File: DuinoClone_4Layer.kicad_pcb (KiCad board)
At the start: 2 copper layers, 41.4 x 27.7 mm, 17 parts, among them J1 Digital pins, J2 Serial, J3 ICSP, J4 I2C, U1 DS1337S+, U2 24LC1025, U3 24LC1025, U4 ATMEGA328P-AU, Y1 Crystal 32MHz, Y2 Crystal 16MHz

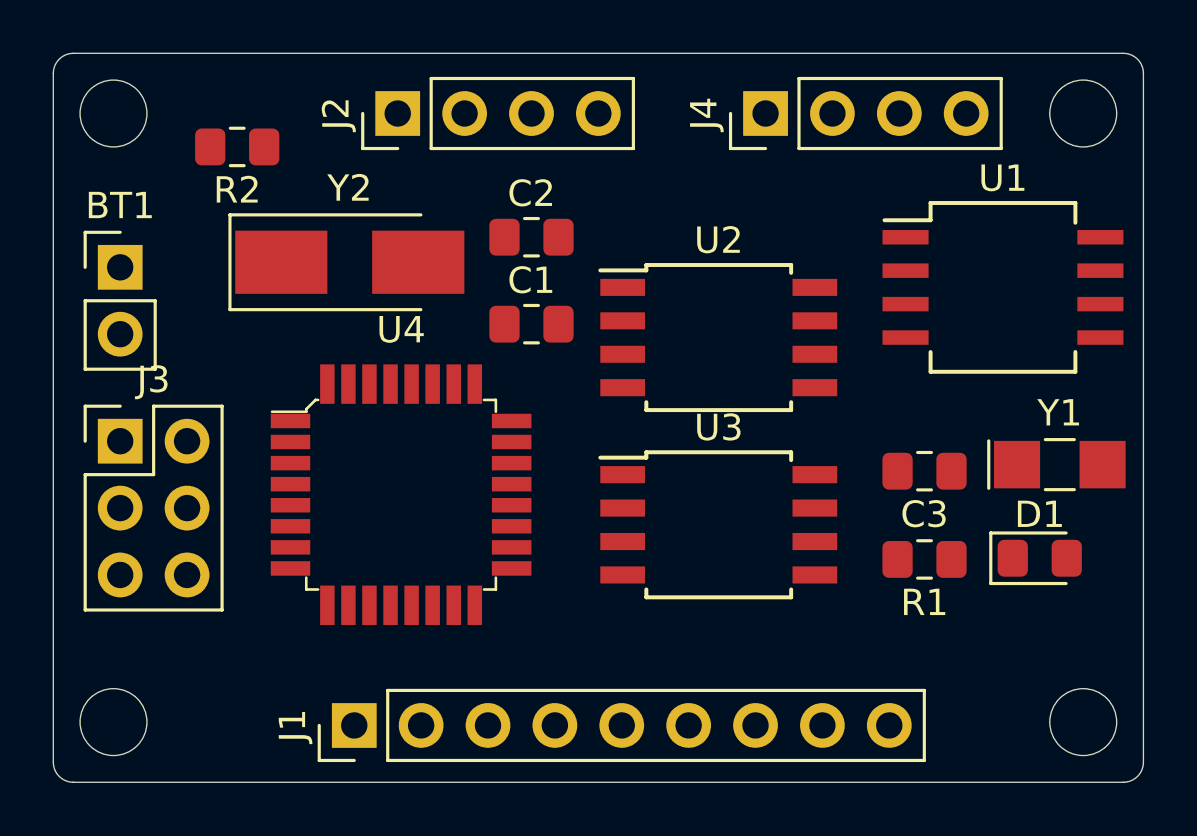
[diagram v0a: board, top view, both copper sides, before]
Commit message: Created copper filled area for 2-layer board
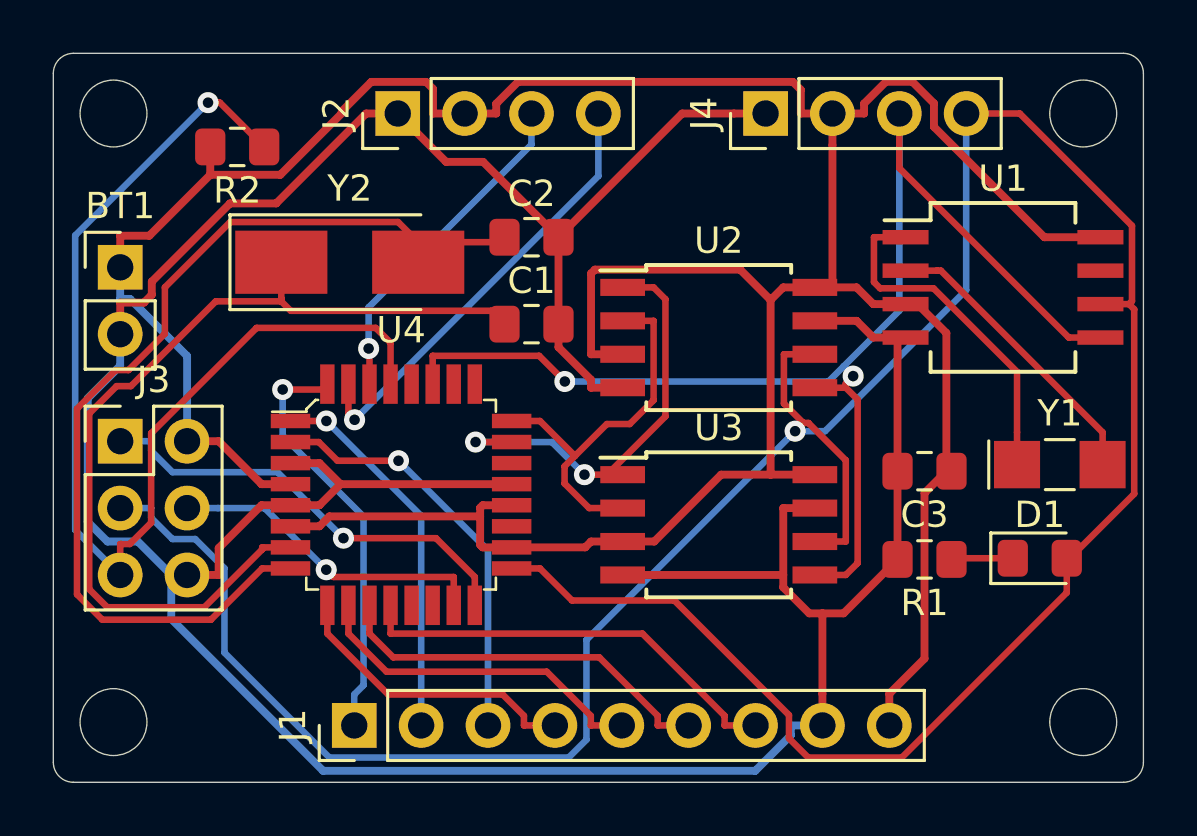
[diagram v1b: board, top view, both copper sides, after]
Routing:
- net /Vcc: track 0.00 -> 133.3 mm
- net GNDPWR: track 0.00 -> 131.2 mm
- net /SCK: track 0.00 -> 116.9 mm, vias 0 -> 1
- net /SDA: track 0.00 -> 51.1 mm, vias 0 -> 2
- net /RESET: track 0.00 -> 42.2 mm, vias 0 -> 1
- net Net-(C2-Pad1): track 0.00 -> 37.7 mm
- net Net-(C1-Pad1): track 0.00 -> 35.0 mm
- net /TX: track 0.00 -> 16.9 mm, vias 0 -> 1
- net /MISO: track 0.00 -> 16.9 mm, vias 0 -> 1
- net /ADDS1: track 0.00 -> 16.9 mm, vias 0 -> 2
- net /D8: track 0.00 -> 16.6 mm
- net /D2: track 0.00 -> 16.0 mm, vias 0 -> 1
- net /D4: track 0.00 -> 15.9 mm, vias 0 -> 1
- net /D7: track 0.00 -> 14.9 mm
- net /ADDS2: track 0.00 -> 14.8 mm
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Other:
- copper layers 2 -> 4
